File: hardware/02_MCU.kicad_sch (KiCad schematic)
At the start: 30 parts, among them SW1 RESET, SW2 BOOT, U6 ESP32-S3-WROOM-1U-N16R8, U7 TPS3808G33-Q1

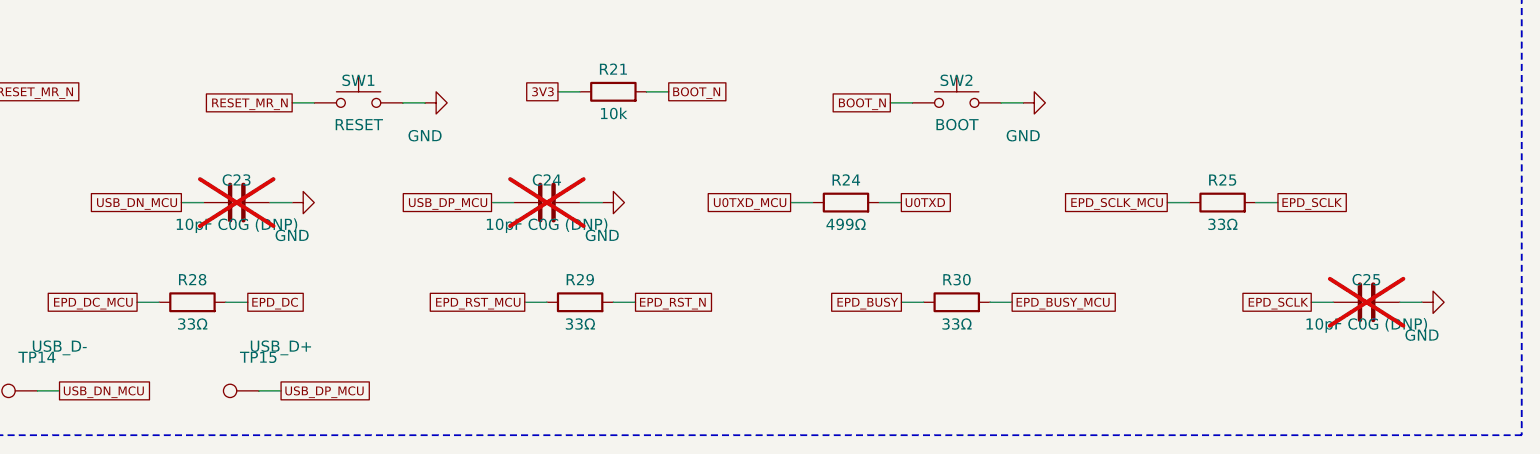
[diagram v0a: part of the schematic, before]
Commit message: Place Rev A board: 4-layer stackup, zones, two-sided placement
Generated by scripts/rebuild/gen_pcb.py from the same circuit definition.
Pre-route DRC: 0 errors, schematic parity: 0 issues.

Co-Authored-By: Claude Opus 5.5 <noreply@anthropic.com>
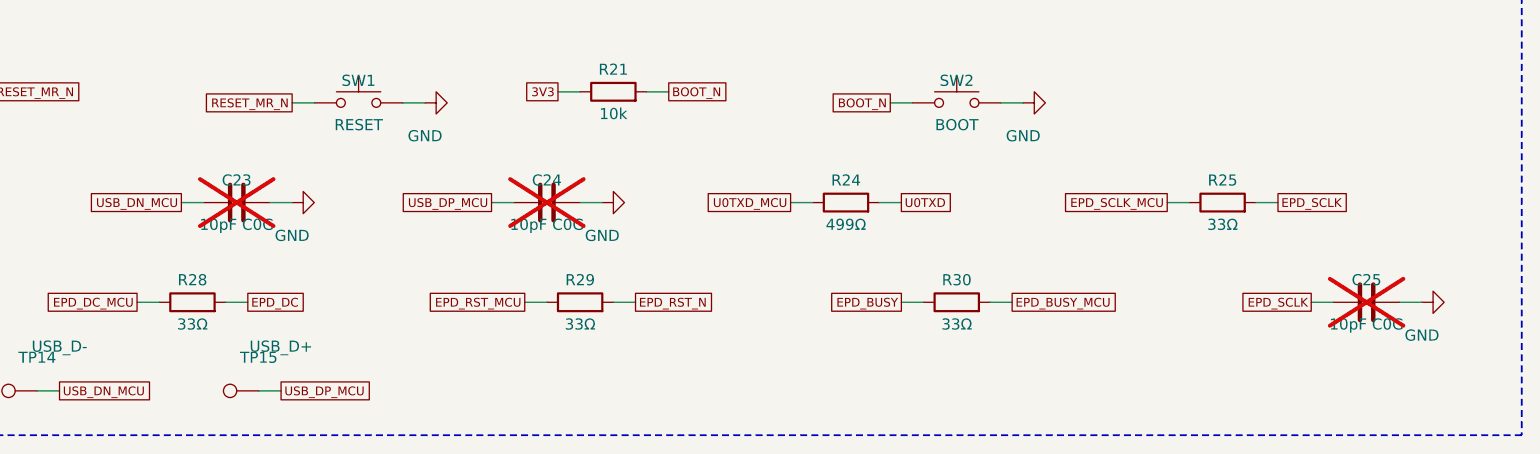
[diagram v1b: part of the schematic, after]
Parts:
- C23, C24, C25: value 10pF C0G (DNP) -> 10pF C0G
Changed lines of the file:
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@@
 			)
 		)
-		(property "Value" "10pF C0G (DNP)"
+		(property "Value" "10pF C0G"
 			(at 134.62 118.11 270)
 			(effects
@@
 			)
 		)
-		(property "Value" "10pF C0G (DNP)"
+		(property "Value" "10pF C0G"
 			(at 170.18 118.11 270)
 			(effects
@@
 			)
 		)
-		(property "Value" "10pF C0G (DNP)"
+		(property "Value" "10pF C0G"
 			(at 264.16 129.54 270)
 			(effects
